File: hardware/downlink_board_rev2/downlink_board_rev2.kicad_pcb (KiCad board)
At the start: 2 copper layers, 65 x 56 mm, 56 parts, among them J1 USB_C_Receptacle_USB2.0, J2 SCREEN, J3 GPIO, J4 PROGRAM, J6 Conn_ST_STDC14, SW1 RPi_{ON}, SW2 RPi_{OFF}, SW3 MCU_{RST}, U1 AZ1117-3.3, U2 TPS563208DDCR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

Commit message: Updated to Rev 2
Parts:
- removed J4: PROGRAM, Connector_PinHeader_2.54mm:PinHeader_1x03_P2.54mm_Vertical
- removed JP2: BOOT0, Connector_PinHeader_2.54mm:PinHeader_1x03_P2.54mm_Vertical
- removed R9: 10k, Resistor_SMD:R_0603_1608Metric
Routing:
- net /BOOT0: track 27.0 -> 0.00 mm, vias 1 -> 0
- net (no net): track 0.00 -> 27.0 mm, vias 0 -> 1
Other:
- board text removed: "BOOT0"
- board text removed: "SWCLK"
- board text removed: "SWDIO"

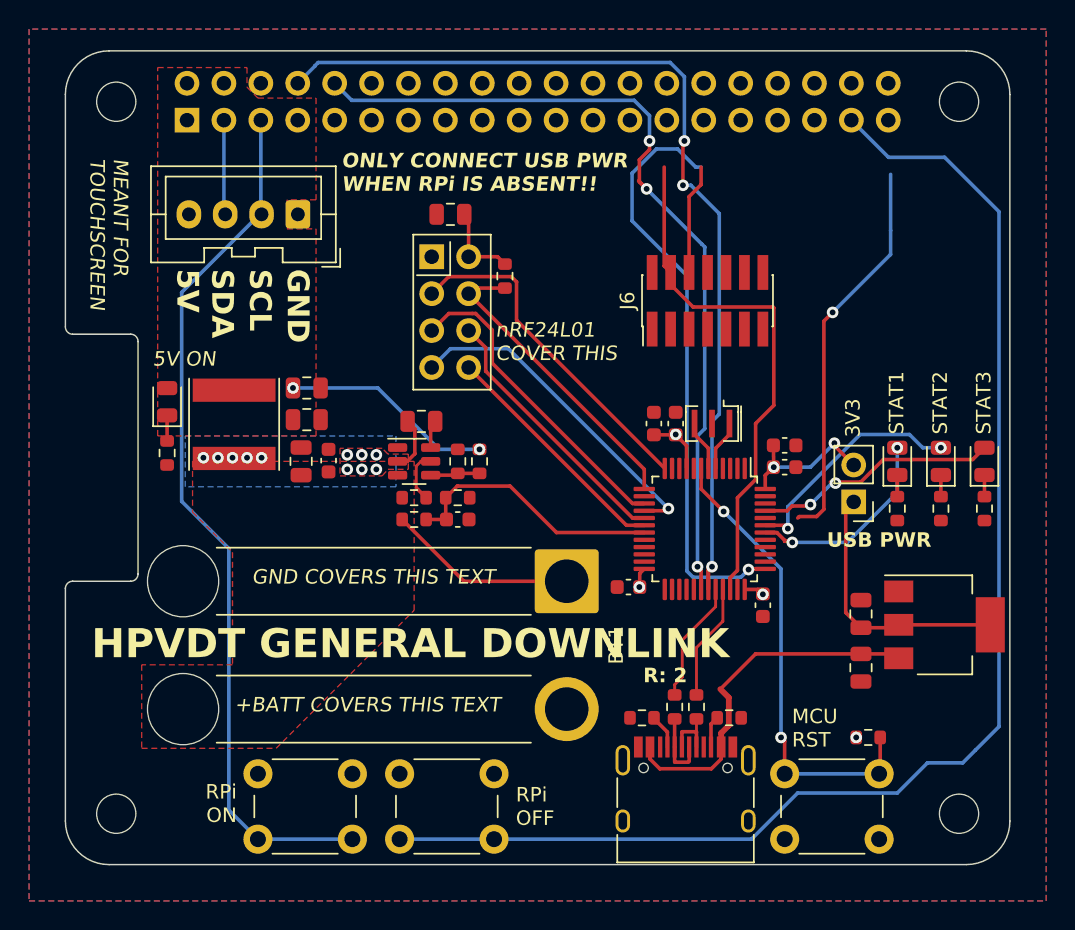
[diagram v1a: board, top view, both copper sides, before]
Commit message: Finished rerouting everything
rerouted everything, resolved the hardware conflict between the header and the NRF module.
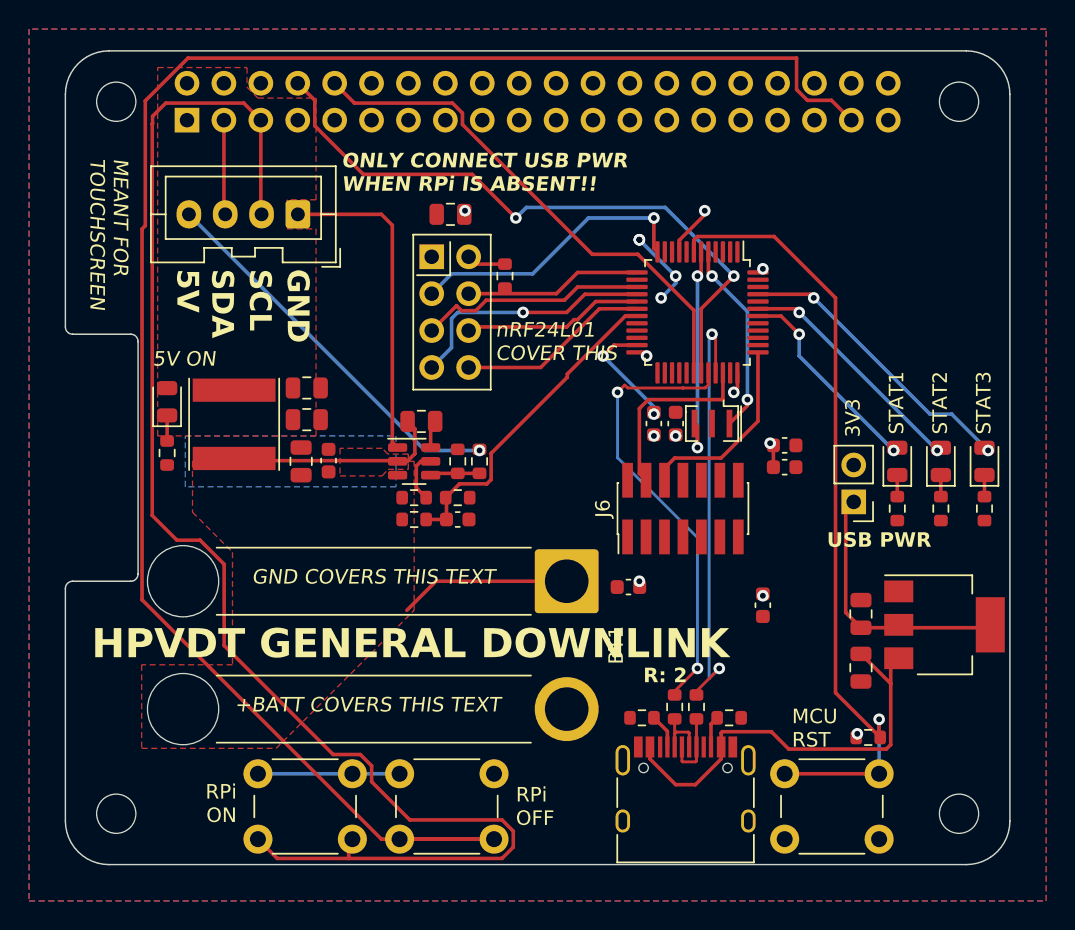
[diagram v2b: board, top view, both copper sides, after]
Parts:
- moved U3 14.9 mm to (143.5, 62.0)
- moved J6 14.4 mm to (142.5, 75.5)
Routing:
- net GND: track 0.00 -> 45.6 mm, vias 0 -> 6
- net /SCL: track 60.5 -> 101.0 mm
- net /SWCLK: track 48.3 -> 13.3 mm, vias 1 -> 0
- net /GPIO26: track 92.7 -> 124.8 mm
- net (no net): track 27.0 -> 0.00 mm, vias 1 -> 0
- net /SDWIO: track 36.7 -> 13.0 mm
- net /RST_{MCU}: track 32.4 -> 55.5 mm, vias 2 -> 1
- net /RPi_{RX}: track 58.4 -> 36.0 mm, vias 3 -> 0
- net /USB_D-: track 8.43 -> 30.5 mm, vias 0 -> 2
- net /USB_D+: track 8.02 -> 30.0 mm, vias 0 -> 2
- net /RPi_{TX}: track 66.2 -> 44.7 mm, vias 3 -> 2
- net +3.3V: track 22.9 -> 9.21 mm, vias 6 -> 11
- net +5V: track 14.7 -> 26.7 mm, vias 2 -> 1
- net Net-(U3-PD1): track 3.48 -> 15.3 mm, vias 0 -> 2
- net Net-(U2-SW): track 3.84 -> 15.2 mm, vias 11 -> 0
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
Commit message: Updated PCB & slight rerouting
Updated PCB to match schematic headers; moved microcontroller closer to USB port
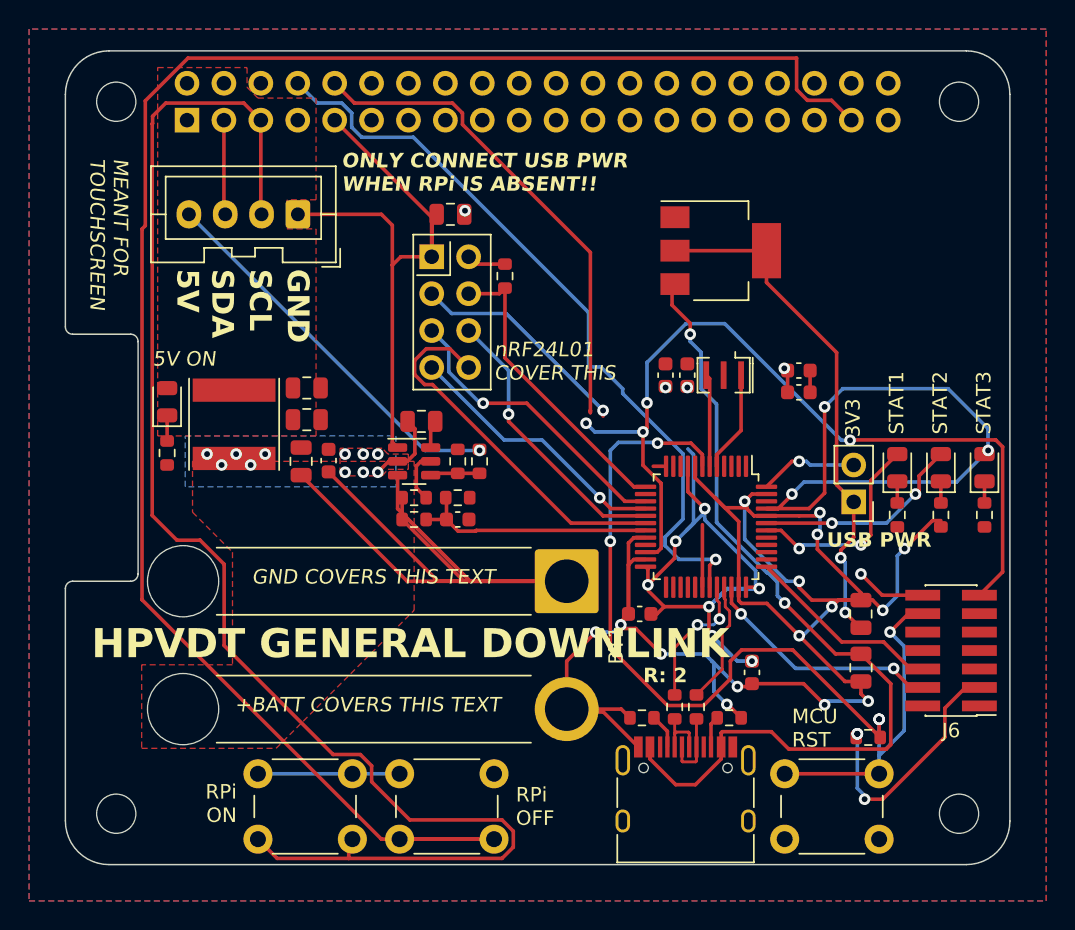
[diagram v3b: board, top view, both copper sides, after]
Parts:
- moved U1 30.0 mm to (145.1, 57.8)
- moved J6 20.9 mm to (160.9, 85.3), turned to 180 degrees
- moved U3 14.8 mm to (144.1, 76.8)
- moved C15 5.24 mm to (150.5, 66.0)
- moved C9 5.24 mm to (150.5, 67.5)
- moved C11 4.69 mm to (147.2, 86.8)
- moved C12 3.43 mm to (142.8, 66.3)
- moved C8 3.43 mm to (141.3, 66.3)
- moved Y1 3.43 mm to (145.3, 66.3)
- moved C10 2.01 mm to (139.5, 82.8)
- moved D1 0.44 mm to (157.2, 72.7)
- moved D3 0.44 mm to (160.2, 72.7)
- moved D4 0.44 mm to (163.2, 72.7)
- moved R11 0.44 mm to (160.2, 75.9)
- moved R12 0.44 mm to (163.2, 75.9)
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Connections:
- J6 pad 11: unconnected-(J6-GNDDetect-Pad11) -> GND
- J6 pad 12: unconnected-(J6-~{RST}-Pad12) -> /RST_{MCU}
- J6 pad 13: unconnected-(J6-VCP_RX-Pad13) -> /Header_{RX}
- J6 pad 14: unconnected-(J6-VCP_TX-Pad14) -> /Header_{TX}
- J6 pad 3: unconnected-(J6-VCC-Pad3) -> +3.3V
- U3 pad 20: GND -> unconnected-(U3-PB2-Pad20)
- U3 pad 21: unconnected-(U3-PB10-Pad21) -> /Header_{TX}
- U3 pad 22: unconnected-(U3-PB11-Pad22) -> /Header_{RX}
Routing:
- net GND: track 45.6 -> 174.7 mm, vias 6 -> 15
- net +BATT: track 11.8 -> 77.6 mm
- net +3.3V: track 9.21 -> 72.5 mm, vias 11 -> 15
- net /Header_{RX}: track 0.00 -> 58.8 mm, vias 0 -> 4
- net Net-(U1-VI): track 30.4 -> 60.7 mm, vias 0 -> 2
- net /USB_D+: track 30.0 -> 8.52 mm, vias 2 -> 0
- net /STATUS_{3}: track 20.3 -> 41.7 mm, vias 2 -> 3
- net /USB_D-: track 30.5 -> 9.42 mm
- net Net-(JP1-A): track 18.3 -> 36.5 mm, vias 0 -> 2
- net /RST_{MCU}: track 55.5 -> 70.3 mm, vias 1 -> 5
- net /RF_{INT}: track 13.3 -> 25.7 mm
- net Net-(U3-PD1): track 15.3 -> 6.37 mm, vias 2 -> 0
- net /RF_{SEL}: track 12.2 -> 20.8 mm
- net /RPi_{TX}: track 44.7 -> 52.8 mm, vias 2 -> 1
- net Net-(U2-SW): track 15.2 -> 8.02 mm, vias 0 -> 11
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
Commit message: Moved caps closer to microcontroller
Moved the four 100nF capacitors closer to the microcontroller (had previously mistakenly moved them farther away)
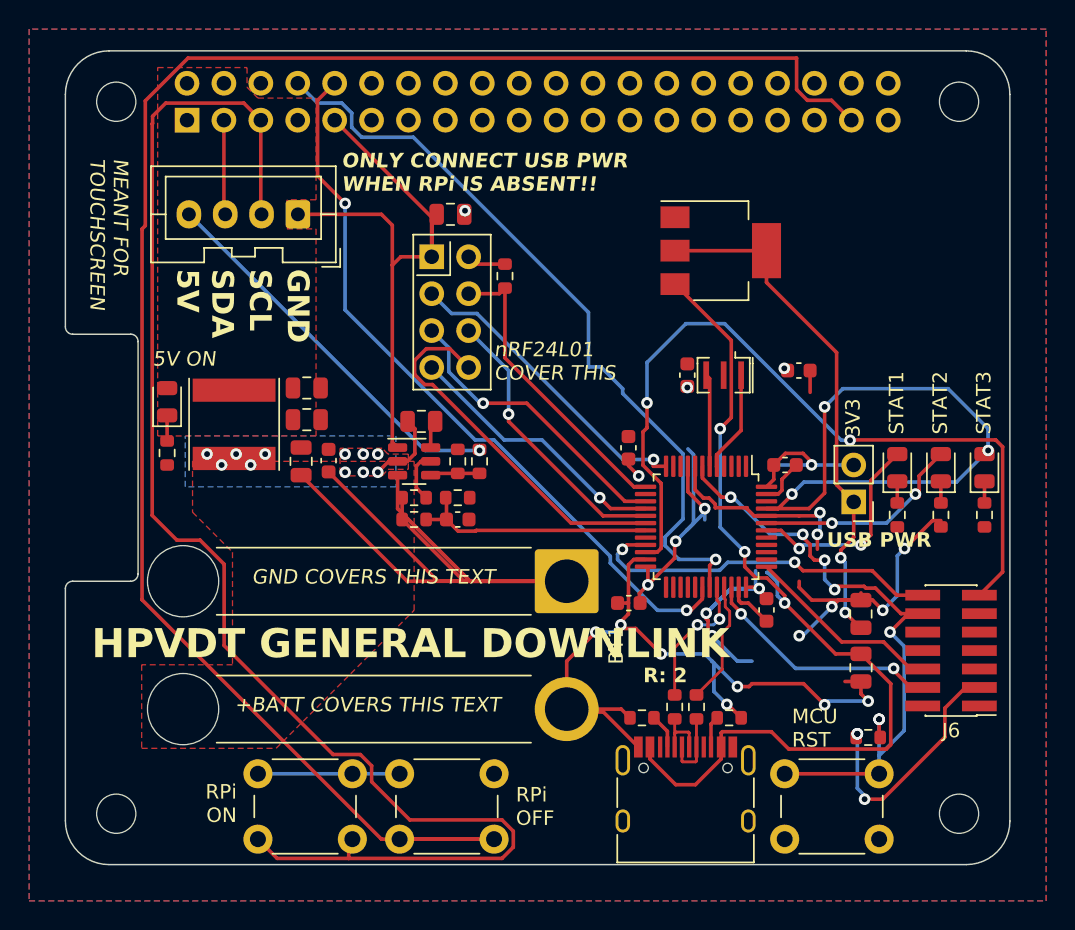
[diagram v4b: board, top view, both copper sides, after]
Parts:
- moved C8 5.61 mm to (138.8, 71.3)
- moved C9 5.09 mm to (149.5, 72.5)
- moved C11 4.41 mm to (148.2, 82.5)
- moved C10 1.06 mm to (138.8, 82.0)
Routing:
- net GND: track 174.7 -> 146.0 mm, vias 15 -> 13
- net /RST_{MCU}: track 70.3 -> 45.3 mm, vias 5 -> 7
- net /Header_{TX}: track 4.85 -> 25.0 mm, vias 1 -> 2
- net /RPi_{RX}: track 38.4 -> 51.4 mm, vias 0 -> 2
- net /RF_{EN}: track 16.4 -> 21.4 mm
- net +3.3V: track 72.5 -> 67.6 mm, vias 15 -> 14
- net /Header_{RX}: track 58.8 -> 54.6 mm, vias 4 -> 2
- net Net-(U1-VI): track 60.7 -> 64.1 mm, vias 2 -> 3
- net Net-(JP1-A): track 36.5 -> 35.7 mm

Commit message: Minor relocation of 10n, 1u caps
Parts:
- moved C12 3.41 mm to (142.8, 69.7)
- moved C15 2.79 mm to (150.0, 68.8)
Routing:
- net +5V: track 26.7 -> 45.3 mm, vias 1 -> 2
- net GND: track 146.0 -> 162.8 mm, vias 13 -> 15
- net +3.3V: track 67.6 -> 72.7 mm, vias 14 -> 13
- net /GPIO26: track 124.8 -> 123.6 mm
